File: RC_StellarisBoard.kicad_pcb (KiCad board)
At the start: 2 copper layers, 54.4 x 55.4 mm, 74 parts, among them K1 CONN_3, K2 CONN_3, K3 CONN_3, K4 CONN_3, K5 CONN_3, K6 CONN_3, P1 CONN_4, P10 XT-60 out, P11 CONN_1, P12 CONN_1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

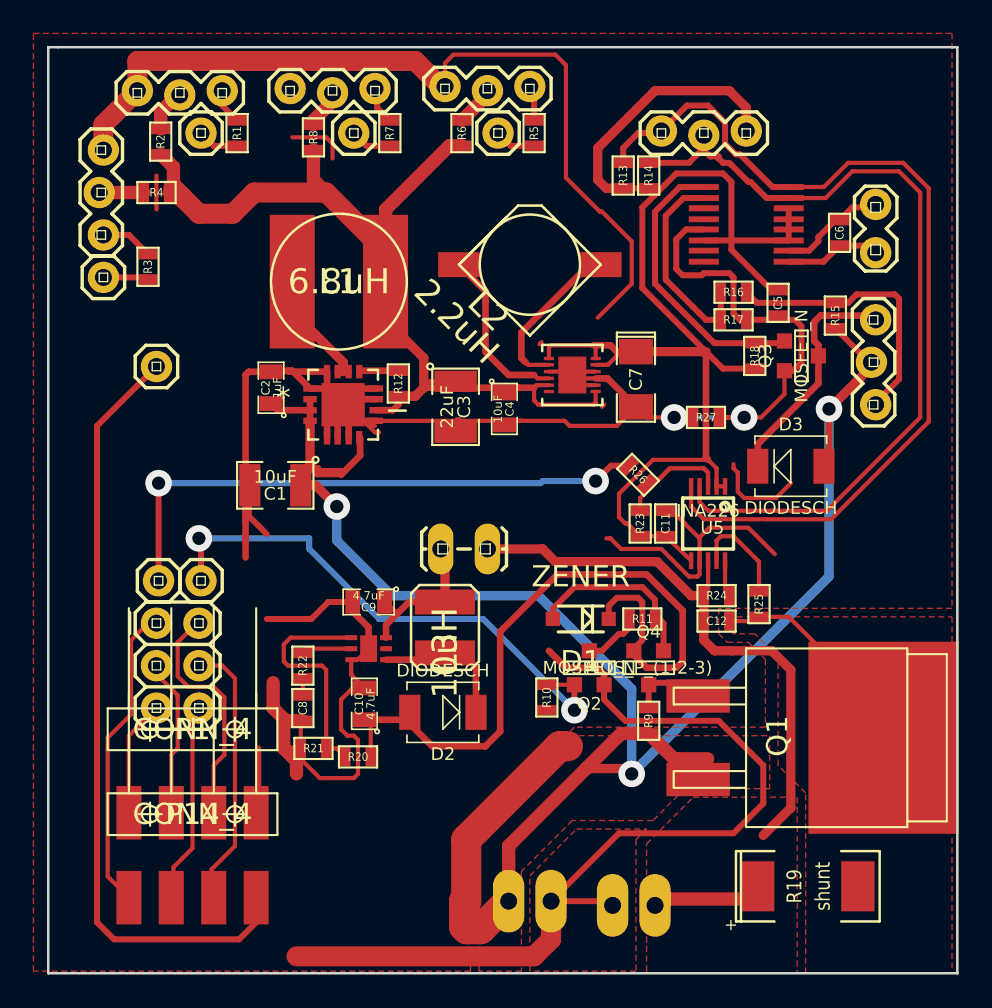
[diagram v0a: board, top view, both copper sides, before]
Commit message: corrigido erro buck boost
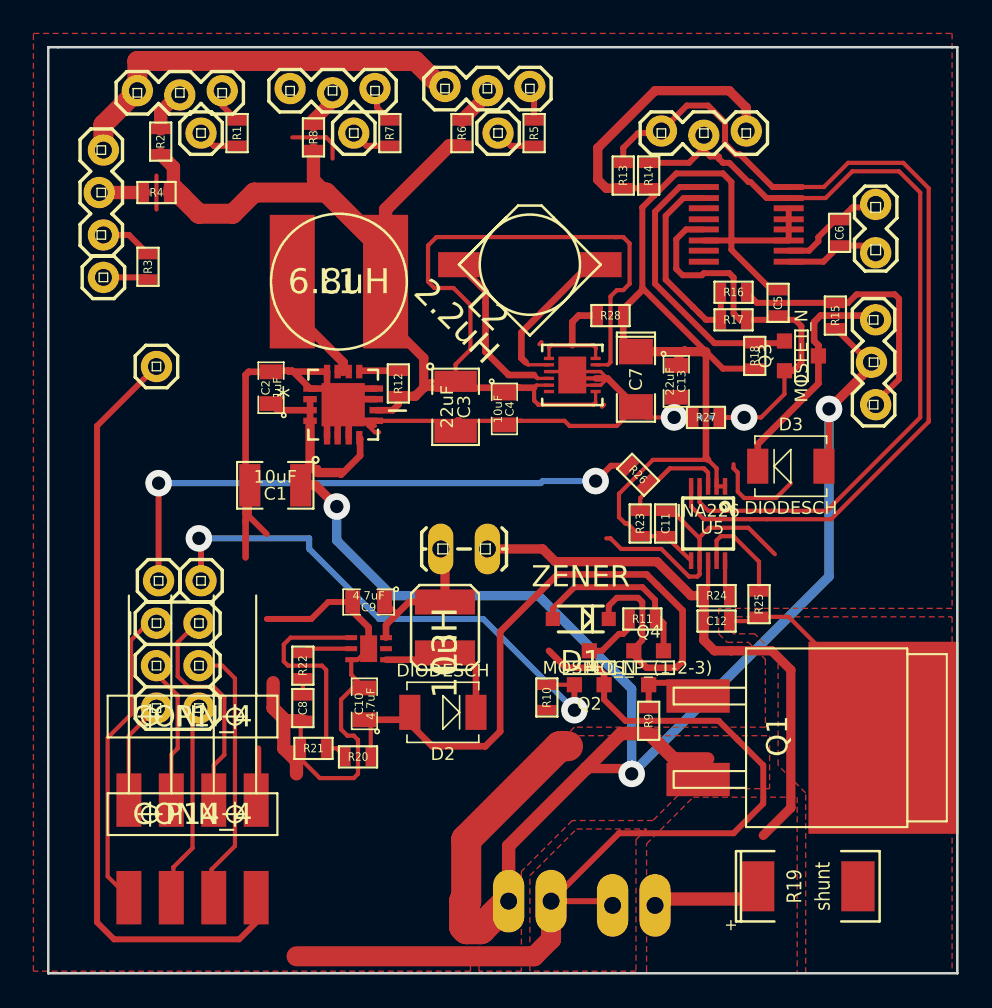
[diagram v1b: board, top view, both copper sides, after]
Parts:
- added C13: 22uF, SM0805, F.Cu at (159.6, 96.9)
- added R28: 0, SM0603, F.Cu at (155.7, 93.0)
- R27: value ina0 -> 0
- moved P1 0.76 mm to (130.7, 117.0)
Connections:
- U3 pad 11: +3.3V -> +5V
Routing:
- net +5V: track 61.6 -> 93.2 mm
- net GND: track 275.8 -> 248.0 mm
- net (no net): track 5.85 -> 11.3 mm
- net +3.3V: track 134.3 -> 139.1 mm
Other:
- rule trace_min: 0.254 -> 0.2

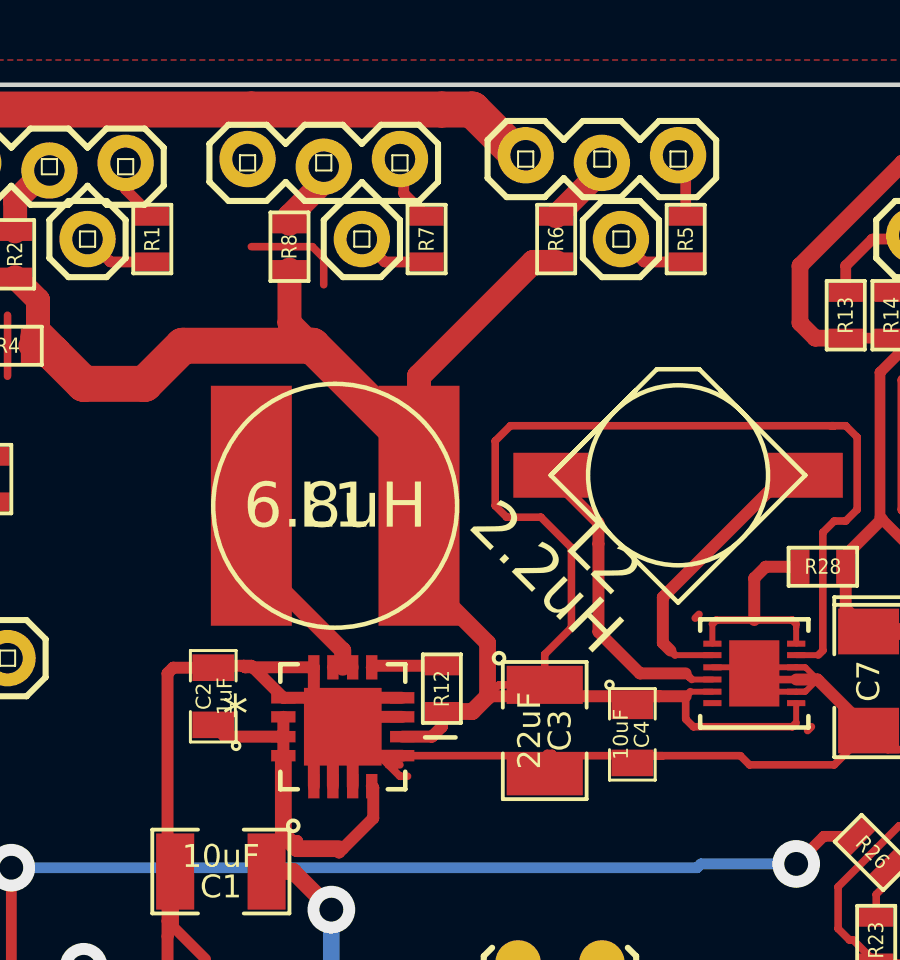
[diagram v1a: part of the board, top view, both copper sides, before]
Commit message: corrigido erro buck boost
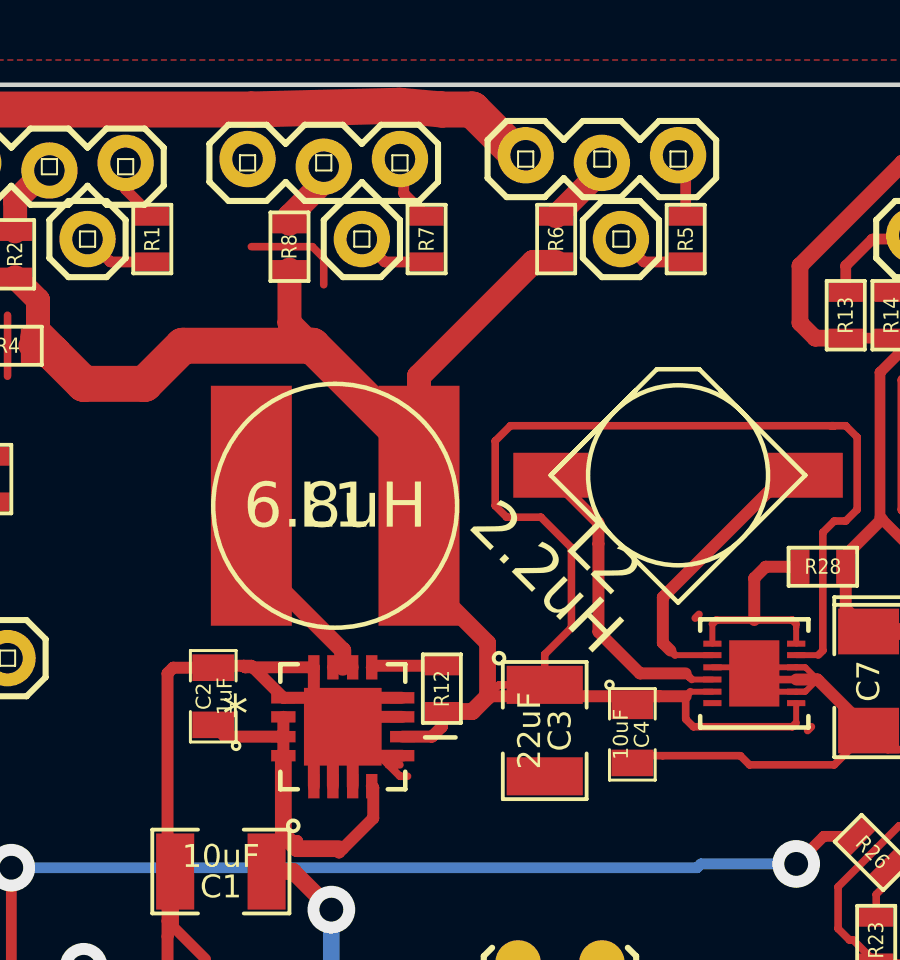
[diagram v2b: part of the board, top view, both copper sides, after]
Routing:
- net GND: track 248.0 -> 238.3 mm
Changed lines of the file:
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@@
     (links 160)
     (no_connects 2)
-    (area 121.971999 76.823499 176.541501 132.409001)
+    (area 91.631431 76.073 182.059917 149.63746)
     (thickness 1.6)
     (drawings 240)
-    (tracks 672)
+    (tracks 667)
     (zones 0)
     (modules 76)
@@
   (segment (start 140.97 117.1575) (end 143.2433 117.1575) (width 0.4) (layer F.Cu) (net 1))
   (segment (start 143.2433 117.1575) (end 143.6878 116.713) (width 0.4) (layer F.Cu) (net 1))
-  (segment (start 159.639 95.9485) (end 159.639 95.631) (width 0.4) (layer F.Cu) (net 2) (status C00000))
-  (segment (start 159.639 95.631) (end 160.147 95.123) (width 0.4) (layer F.Cu) (net 2) (status 400000))
+  (segment (start 159.639 95.9485) (end 159.639 95.631) (width 0.4) (layer F.Cu) (net 2))
+  (segment (start 159.639 95.631) (end 160.147 95.123) (width 0.4) (layer F.Cu) (net 2))
   (segment (start 160.147 95.123) (end 160.147 94.996) (width 0.4) (layer F.Cu) (net 2))
   (segment (start 160.147 94.996) (end 160.147 95.123) (width 0.4) (layer F.Cu) (net 2))
@@
   (segment (start 127 112.395) (end 127 116.84) (width 0.254) (layer F.Cu) (net 21))
   (segment (start 128.016 111.379) (end 127 112.395) (width 0.254) (layer F.Cu) (net 21))
-  (segment (start 159.639 97.8535) (end 159.639 98.933) (width 0.4) (layer F.Cu) (net 22) (status 400000))
+  (segment (start 159.639 97.8535) (end 159.639 98.933) (width 0.4) (layer F.Cu) (net 22))
   (segment (start 159.639 98.933) (end 159.512 99.06) (width 0.4) (layer F.Cu) (net 22))
   (segment (start 152.019 96.3168) (end 153.2128 96.3168) (width 0.2) (layer F.Cu) (net 22))
@@
   (segment (start 144.018 77.724) (end 145.796 79.502) (width 1.2) (layer F.Cu) (net 22))
   (segment (start 127.381 77.724) (end 136.652 77.724) (width 1.2) (layer F.Cu) (net 22))
-  (segment (start 136.652 77.724) (end 143.002 77.724) (width 1.2) (layer F.Cu) (net 22))
+  (segment (start 136.652 77.724) (end 141.605 77.597) (width 1.2) (layer F.Cu) (net 22))
+  (segment (start 141.605 77.597) (end 143.002 77.724) (width 1.2) (layer F.Cu) (net 22))
   (segment (start 127.381 79.502) (end 127.381 77.724) (width 1.2) (layer F.Cu) (net 22))
   (segment (start 160.147 105.41) (end 159.639 104.902) (width 0.254) (layer F.Cu) (net 22))
@@
   (segment (start 150.368 99.2632) (end 149.5933 99.2632) (width 0.254) (layer F.Cu) (net 22))
   (segment (start 149.5933 99.2632) (end 149.352 99.5045) (width 0.254) (layer F.Cu) (net 22))
-  (segment (start 146.431 99.949) (end 146.431 99.2632) (width 0.254) (layer F.Cu) (net 22))
-  (segment (start 146.685 99.187) (end 146.685 99.2632) (width 0.254) (layer F.Cu) (net 22))
-  (segment (start 146.5072 99.187) (end 146.685 99.187) (width 0.254) (layer F.Cu) (net 22))
-  (segment (start 146.431 99.2632) (end 146.5072 99.187) (width 0.254) (layer F.Cu) (net 22))
-  (segment (start 141.6812 99.2632) (end 146.685 99.2632) (width 0.254) (layer F.Cu) (net 22))
-  (segment (start 146.685 99.2632) (end 150.368 99.2632) (width 0.254) (layer F.Cu) (net 22))
   (segment (start 150.368 99.2632) (end 152.951802 99.2632) (width 0.254) (layer F.Cu) (net 22))
   (segment (start 156.083 99.568) (end 157.226 98.425) (width 0.254) (layer F.Cu) (net 22))

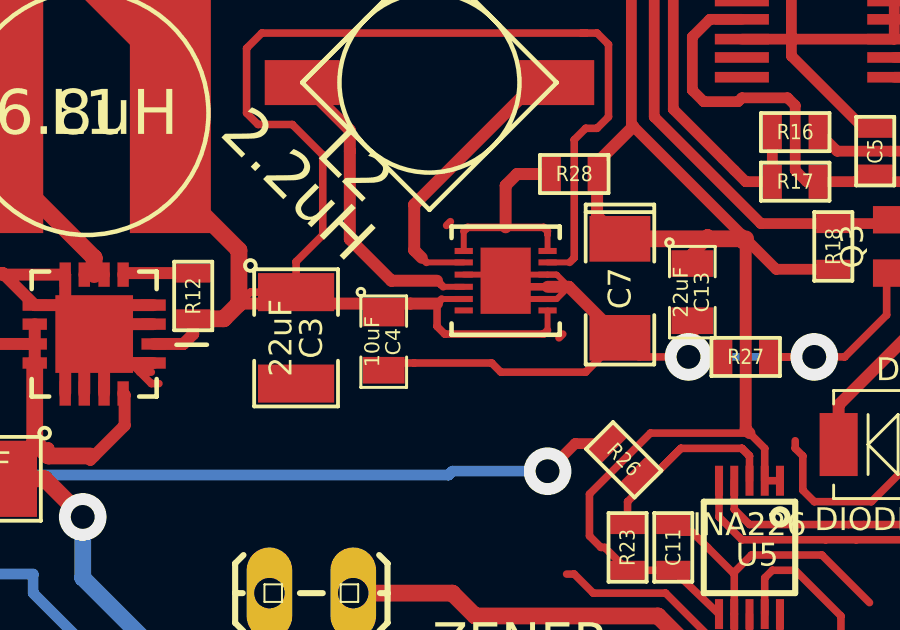
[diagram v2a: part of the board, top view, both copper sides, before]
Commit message: corrigido erro buck boost 1
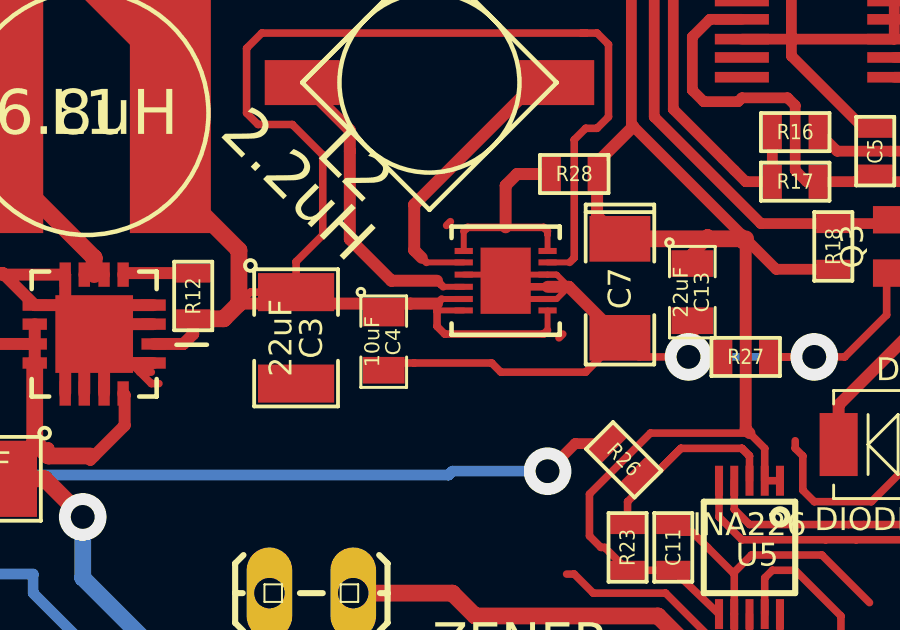
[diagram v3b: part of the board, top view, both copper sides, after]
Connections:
- U3 pad 6: N-0000056 -> +5V
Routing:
- net +5V: track 93.2 -> 94.1 mm

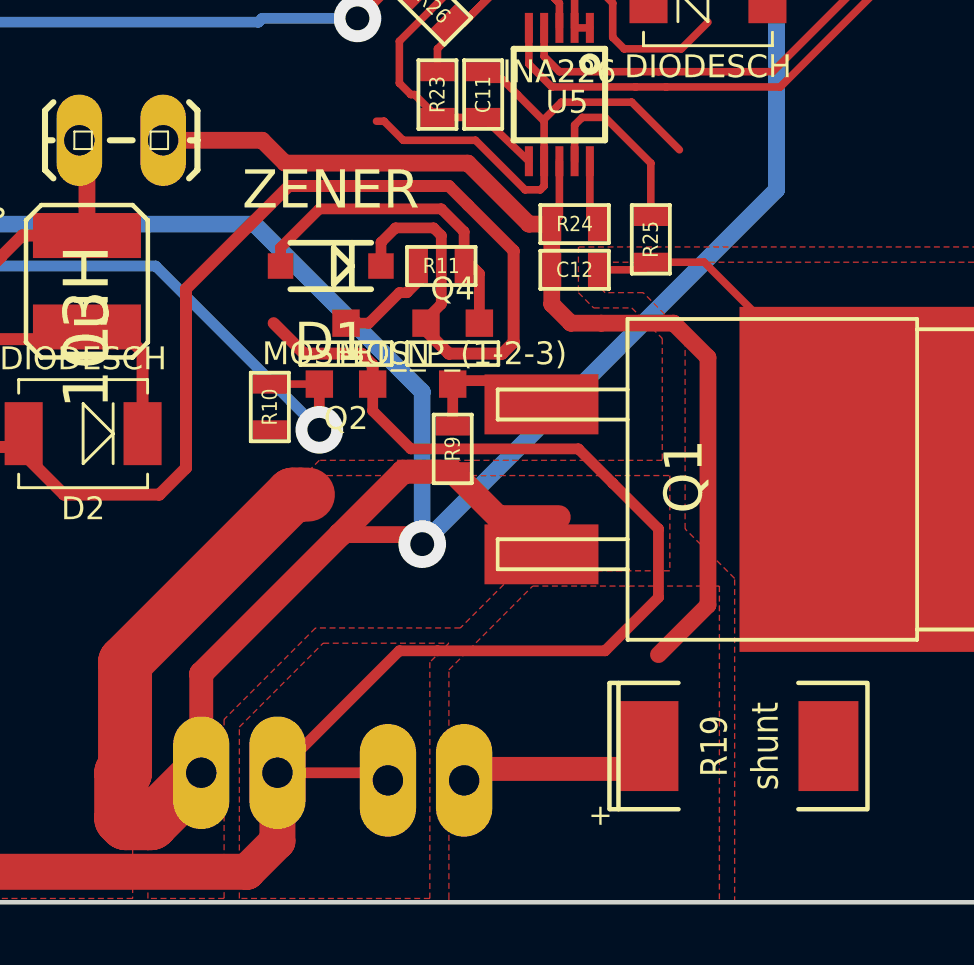
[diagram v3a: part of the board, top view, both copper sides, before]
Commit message: resist mosfet P done
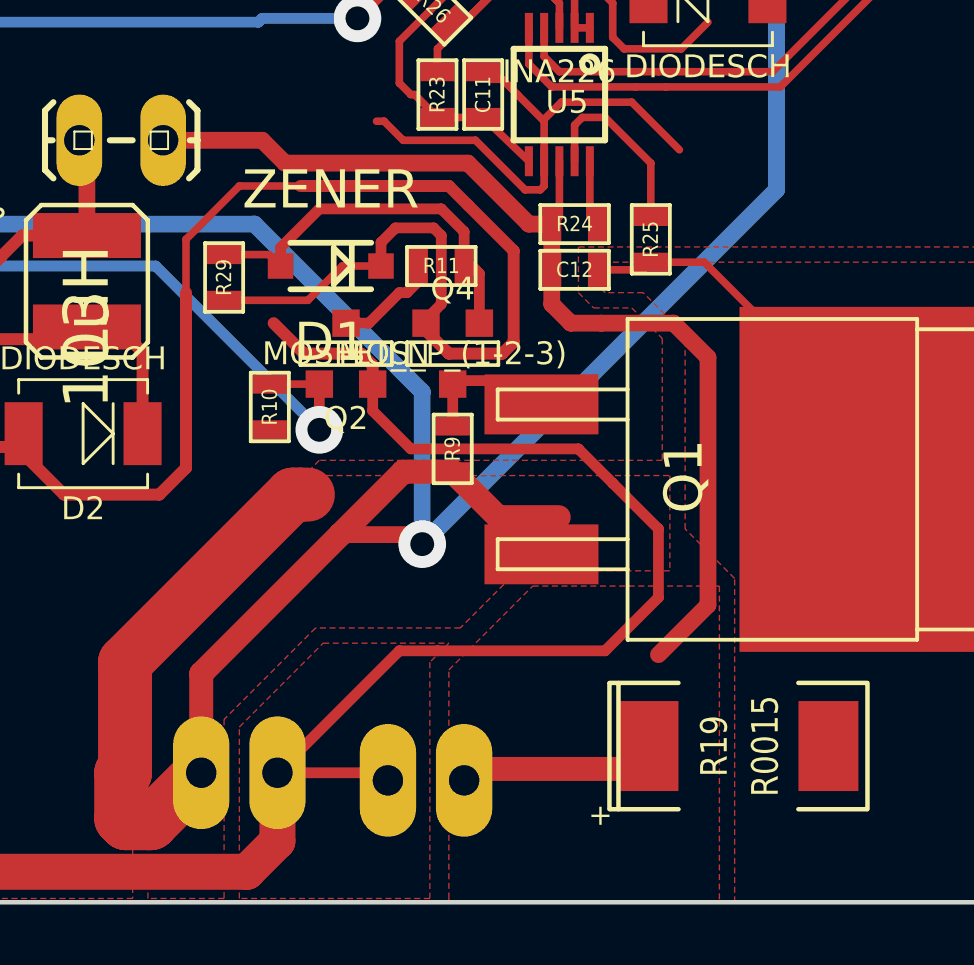
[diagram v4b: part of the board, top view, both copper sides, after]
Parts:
- added R29: 22K, SM0603, F.Cu at (150.4, 111.5)
- C12: value 0.1uF -> 0.01uF
- C7: value 22uF -> 4u7
- R1, R11, R3, R5, R7: value R -> 100R
- R10: value R -> 4k7
- R19: value shunt -> R0015
- R2, R4, R6, R8: value R -> 0
- R24, R25: value 10k -> 10R
- R26: value ina0 -> 0R
- R9: value R -> 22k
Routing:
- net +24V: track 43.9 -> 50.6 mm
- net N-0000028: track 11.0 -> 13.0 mm
